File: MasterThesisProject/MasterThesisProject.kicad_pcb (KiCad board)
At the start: 2 copper layers, 99.1 x 99.1 mm, 44 parts, among them J1 Conn_01x07_Male, SW1 SW_MEC_5E, U1 LCD_I2C, U10 TGS5342, U11 CDM7160, U12 INA128, U13 LM4041AILT-1.2, U14 LPS331PA_Module, U2 SensironSPS30, U3 LM317_TO-220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

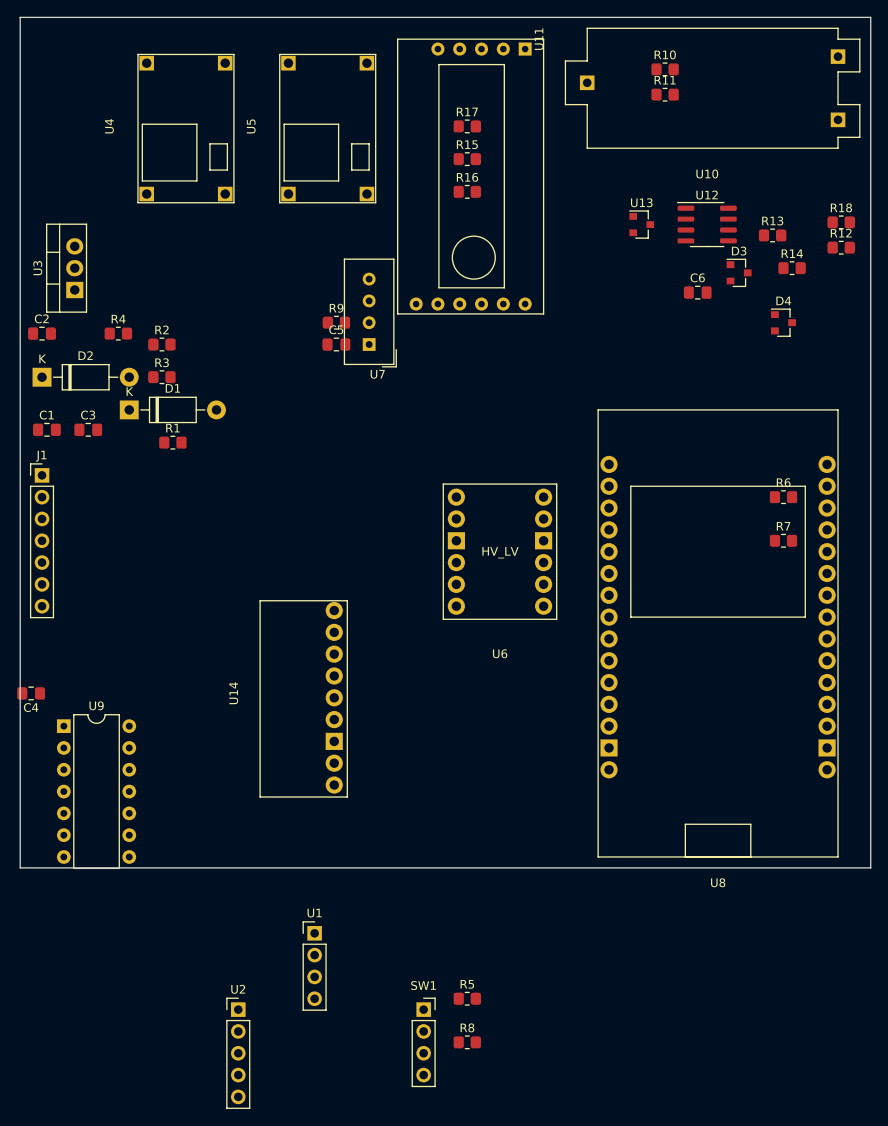
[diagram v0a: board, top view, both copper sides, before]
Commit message: Connect all elements to GND, minor updates to schematic
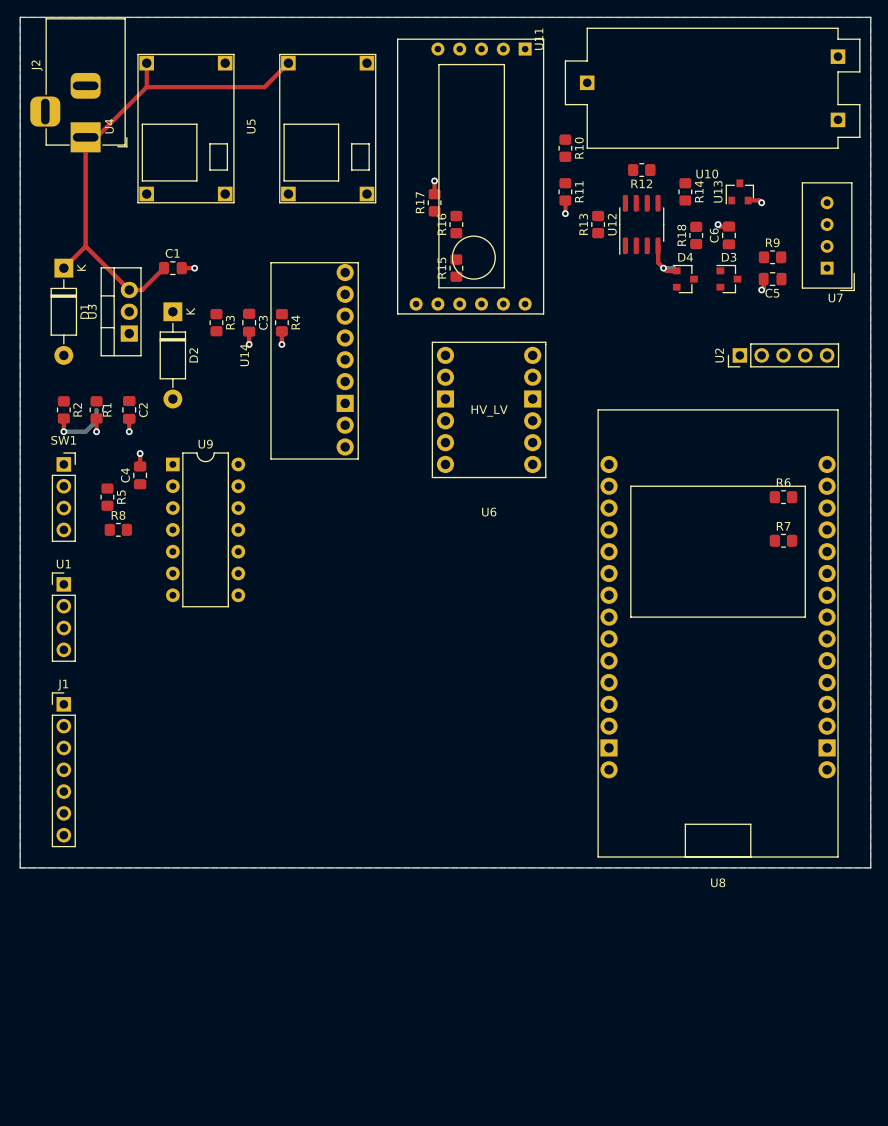
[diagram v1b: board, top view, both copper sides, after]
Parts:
- added J2: Barrel_Jack, Connector_BarrelJack:BarrelJack_Horizontal, F.Cu at (45.7, 80.0)
- moved U2 96.0 mm to (121.9, 105.4), turned to 90 degrees
- moved SW1 76.1 mm to (43.2, 118.1)
- moved R8 72.2 mm to (49.5, 125.7)
- moved R5 71.9 mm to (48.3, 121.9), turned to 270 degrees
- moved U7 54.1 mm to (132.1, 95.2)
- moved C5 51.4 mm to (125.7, 96.5), turned to 180 degrees
- moved R9 51.4 mm to (125.7, 94.0)
- moved U1 50.0 mm to (43.2, 132.1)
- moved U14 39.4 mm to (64.8, 105.4)
- moved U9 33.0 mm to (55.9, 118.1)
- moved C4 28.4 mm to (52.1, 119.4), turned to 90 degrees
- moved J1 26.8 mm to (43.2, 146.1)
- moved R12 24.9 mm to (110.5, 83.8), turned to 180 degrees
- moved C1 23.9 mm to (55.9, 95.2)
- moved C3 22.5 mm to (64.8, 101.6), turned to 270 degrees
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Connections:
- R5 pad 1: Net-(R5-Pad1) -> +3V3
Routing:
- net +9V: track 0.00 -> 58.6 mm
- net GND: track 0.00 -> 29.1 mm, vias 0 -> 13
- added copper zone on B.Cu, net GND

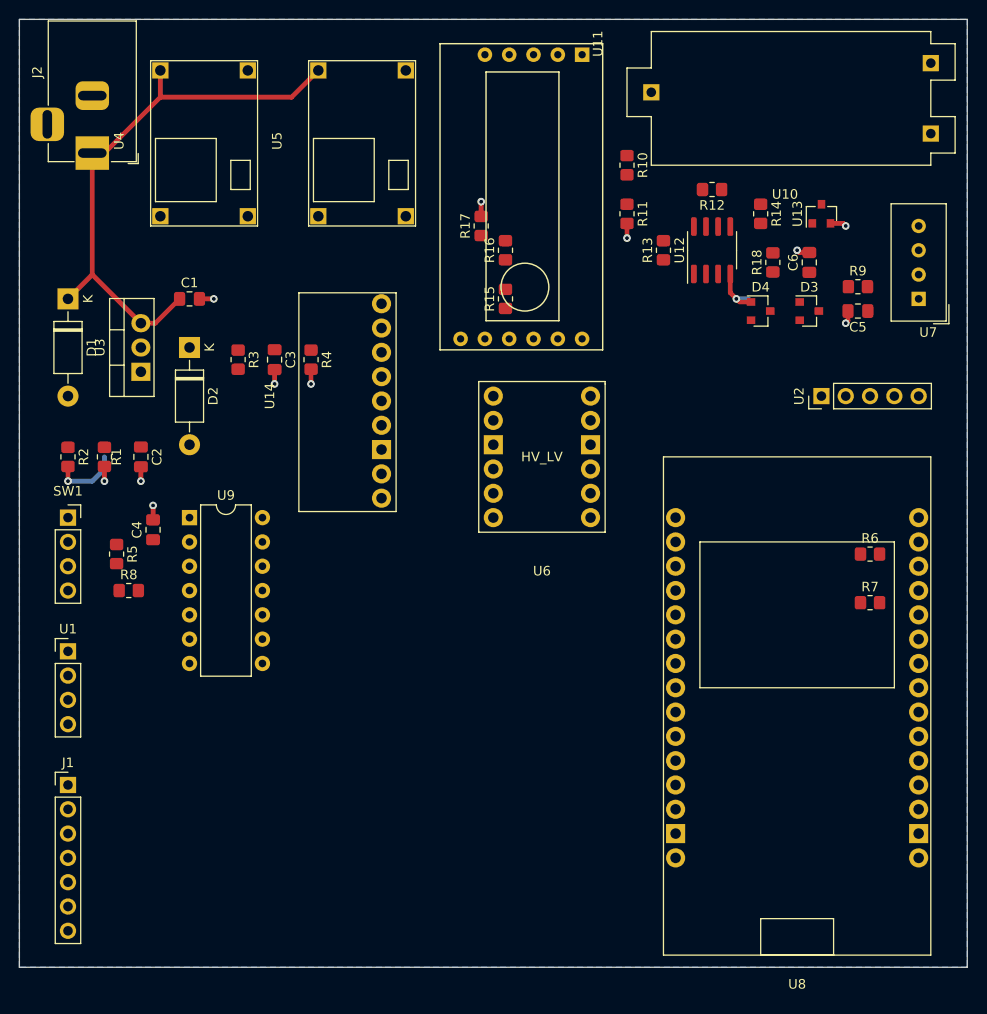
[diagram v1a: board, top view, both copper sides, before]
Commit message: Add all missing connections to pcb
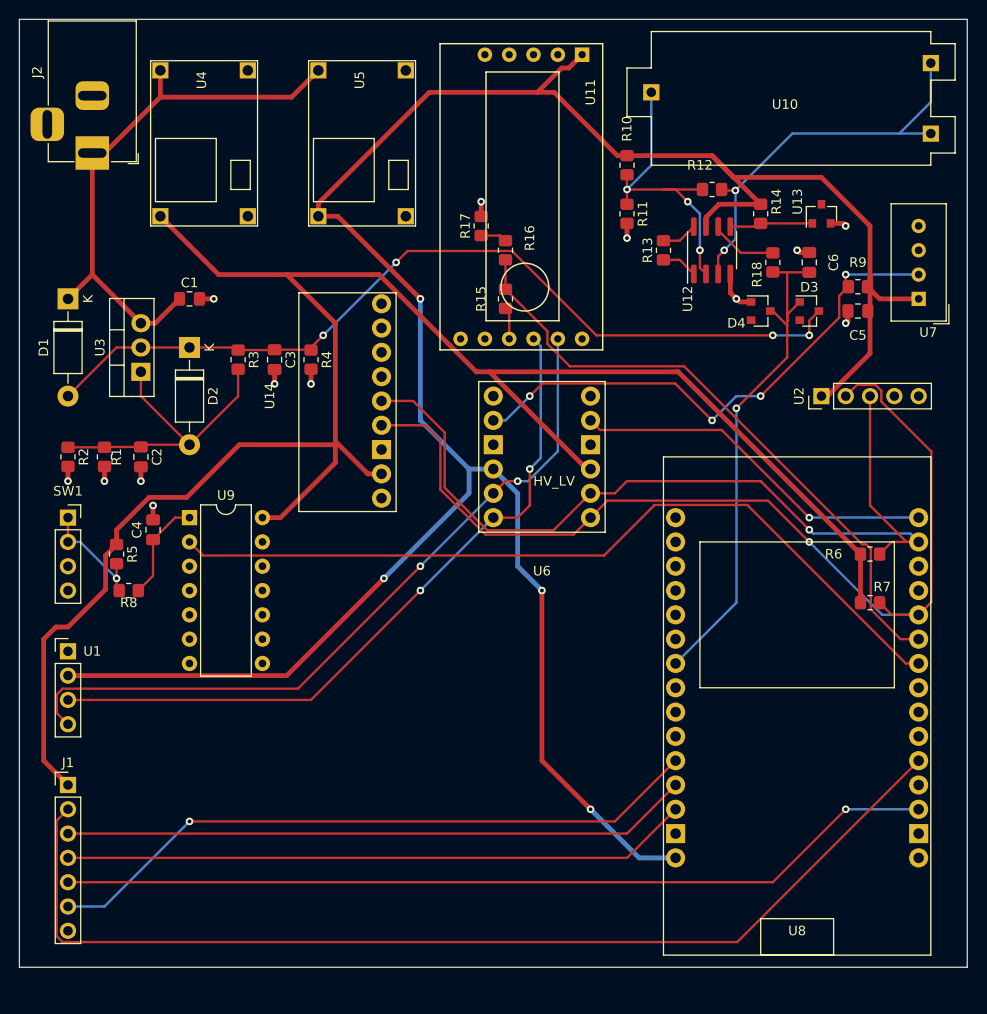
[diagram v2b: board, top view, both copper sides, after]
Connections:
- U8 pad 13: Net-(U8-Pad13) -> GND
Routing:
- net +5V: track 0.00 -> 257.9 mm, vias 0 -> 4
- net +3V3: track 0.00 -> 203.8 mm
- net ETH_INT: track 0.00 -> 111.9 mm
- net SDA: track 0.00 -> 105.5 mm, vias 0 -> 1
- net SPI_CS: track 0.00 -> 92.1 mm, vias 0 -> 1
- net SCL: track 0.00 -> 91.3 mm, vias 0 -> 1
- net +3V0: track 0.00 -> 90.8 mm, vias 0 -> 4
- net LCD_BUTTON: track 0.00 -> 85.8 mm
- net SCL_HIGH: track 0.00 -> 78.2 mm, vias 0 -> 2
- net SDA_HIGH: track 0.00 -> 74.9 mm, vias 0 -> 2
- net SPI_CLK: track 0.00 -> 69.8 mm, vias 0 -> 1
- net CO2_BUSY: track 0.00 -> 65.9 mm
- net SPI_MOSI: track 0.00 -> 65.6 mm
- net SPI_MISO: track 0.00 -> 65.6 mm
- net DHT_HIGH: track 0.00 -> 56.4 mm, vias 0 -> 4
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- removed copper zone on B.Cu, net GND

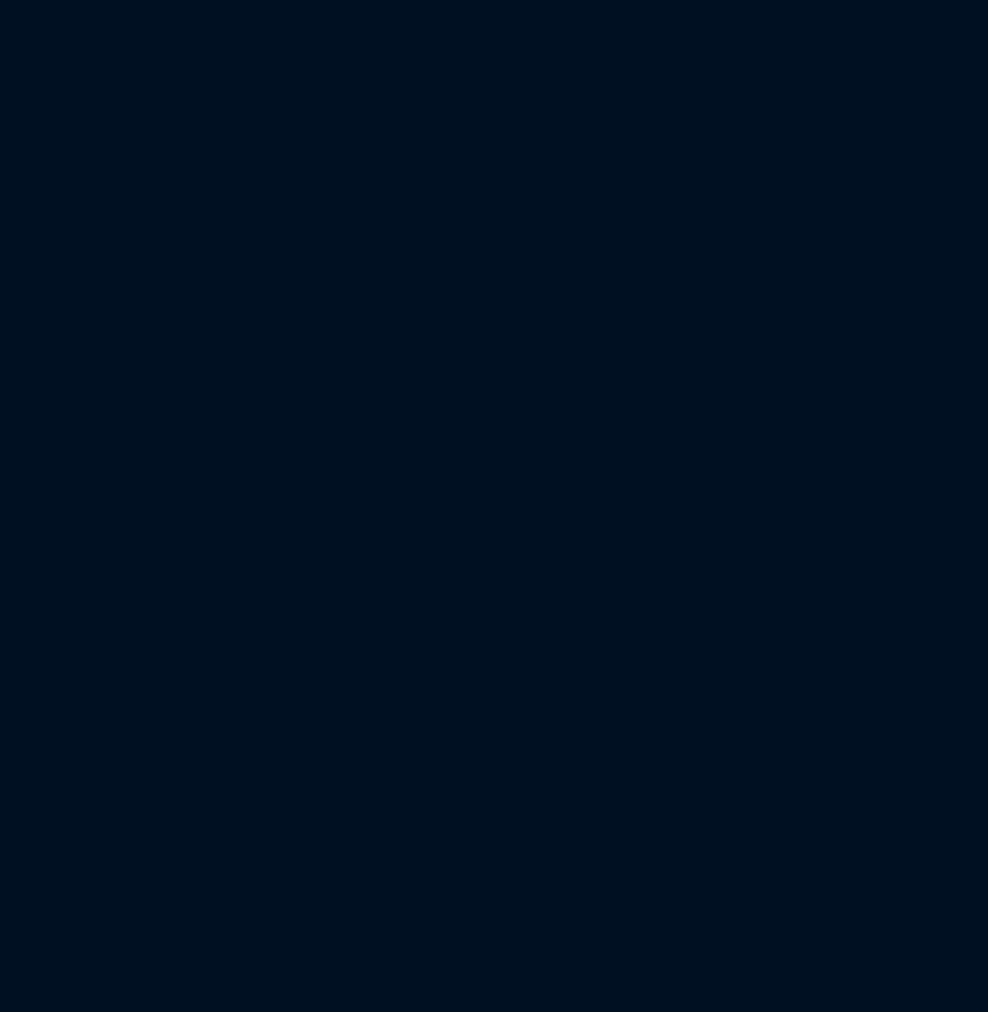
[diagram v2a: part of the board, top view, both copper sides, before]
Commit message: Add new pcb edges
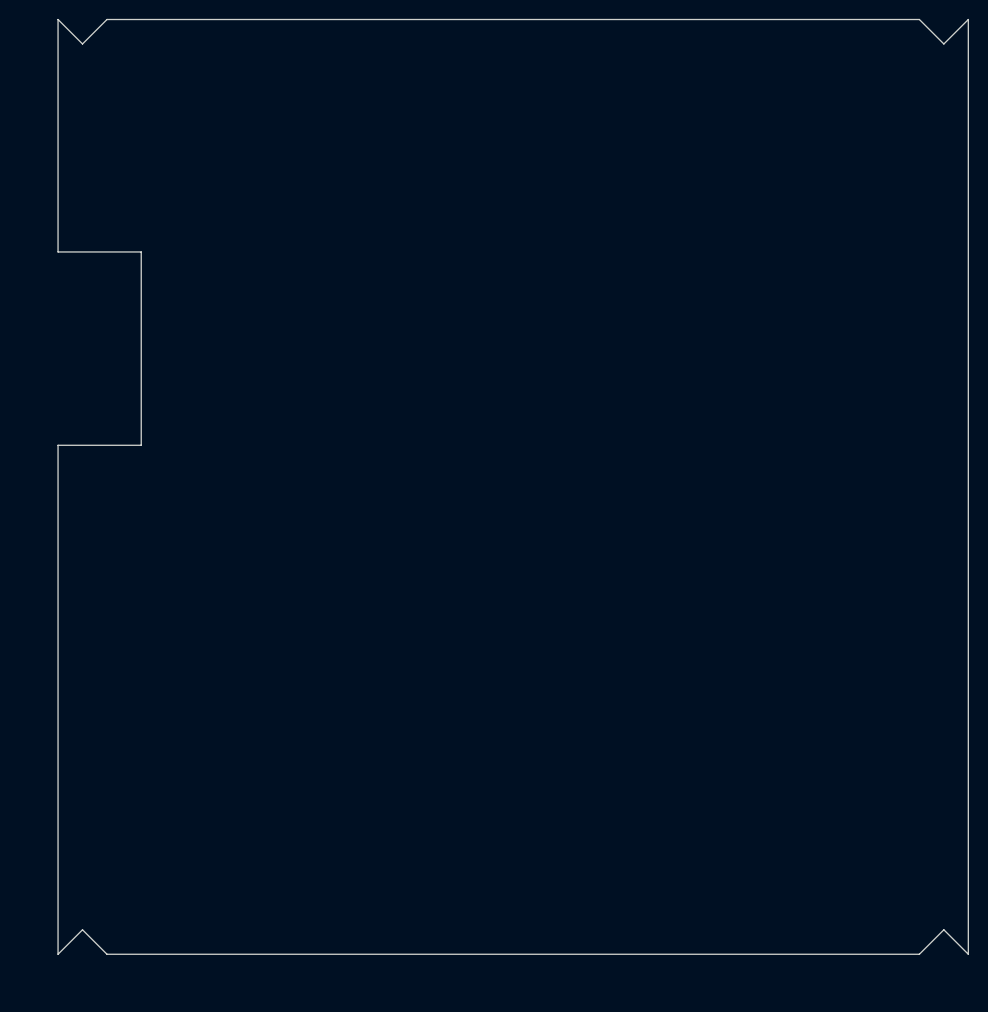
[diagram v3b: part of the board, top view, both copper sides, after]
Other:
- board size 99.1 x 99.1 mm -> 227.1 x 129.8 mm
